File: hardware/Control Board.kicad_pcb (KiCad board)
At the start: 2 copper layers, 68.4 x 53.1 mm, 38 parts, among them J1 Conn_FTDI, J2 SOLAR, M1 Motor_DC, Q1 IRF7105PbF, Q2 BC817W, Q3 BC817W, Q4 IRF7105PbF, SW1 SW_Push, SW2 SW_Push, SW3 SW_Push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

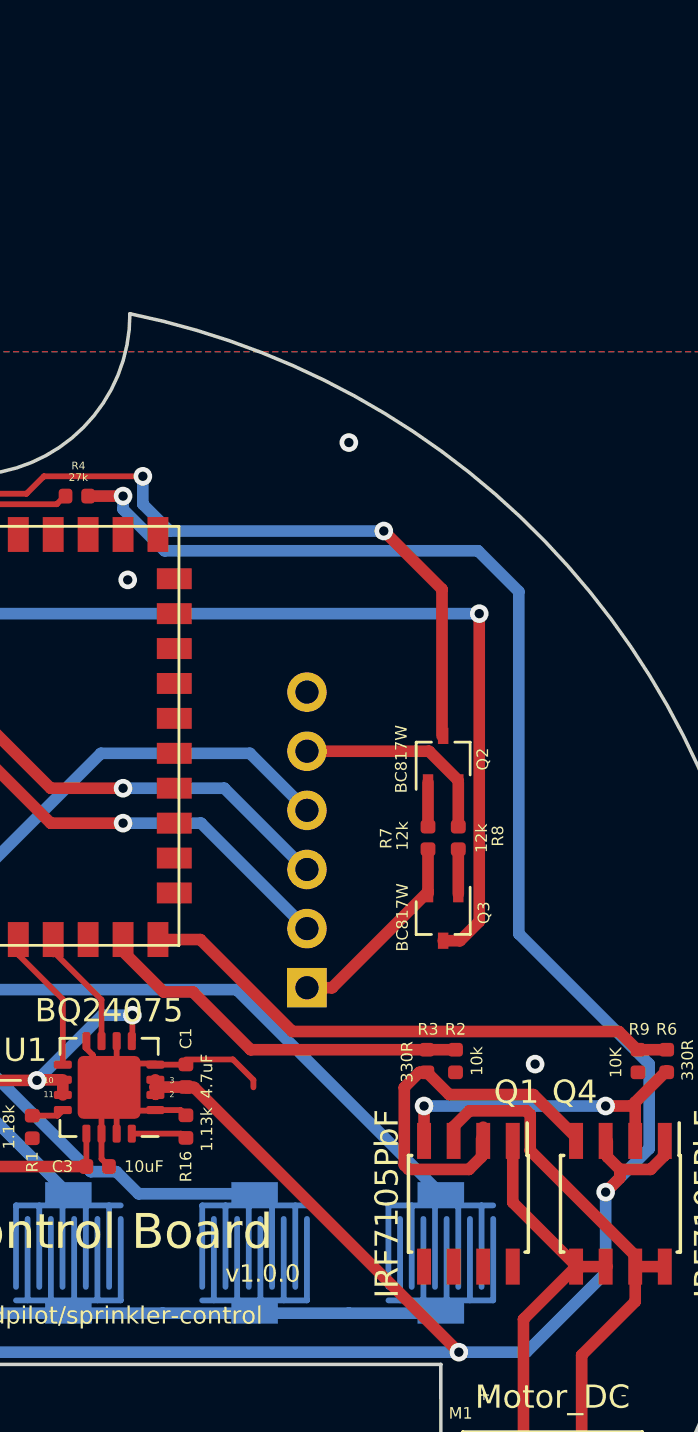
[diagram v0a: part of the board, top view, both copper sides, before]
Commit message: Add pull up resistors on the auto programmer circuit, switch the RX and TX lines
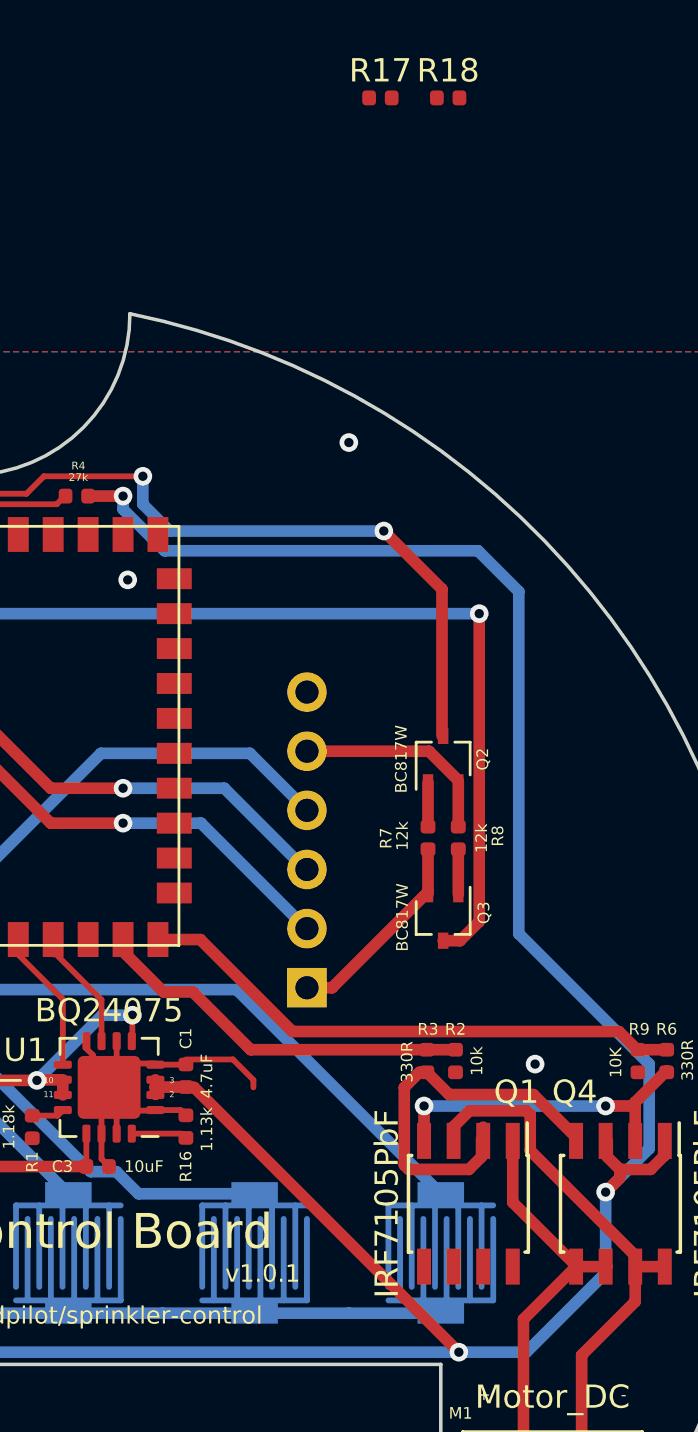
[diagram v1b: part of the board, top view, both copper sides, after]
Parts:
- added R17: 10k, Resistor_SMD:R_0402_1005Metric, F.Cu at (126.7, 87.6)
- added R18: 10k, Resistor_SMD:R_0402_1005Metric, F.Cu at (129.6, 87.6)
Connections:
- U3 pad 37: TX -> RX
- U3 pad 38: RX -> TX
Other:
- board text added: "v1.0.1"
- board text removed: "v1.0.0"
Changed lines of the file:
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@@
     (tracks 258)
     (zones 0)
-    (modules 38)
+    (modules 40)
     (nets 54)
   )
@@
     (add_net WATER_ON)
   )
+  (module Resistor_SMD:R_0402_1005Metric (layer F.Cu)
+    (at 129.565001 87.595001)
+    (descr "Resistor SMD 0402 (1005 Metric), square (rectangular) end terminal, IPC_7351 nominal, (Body size source: http://www.tortai-tech.com/upload/download/2011102023233369053.pdf), generated with kicad-footprint-generator")
+    (tags resistor)
+    (attr smd)
+    (fp_text reference R18 (at 0 -1.17) (layer F.SilkS)
+      (effects (font (size 1 1) (thickness 0.15)))
+    )
+    (fp_text value 10k (at 0 1.17) (layer F.Fab)
+      (effects (font (size 1 1) (thickness 0.15)))
+    )
+    (fp_text user %R (at 0 0) (layer F.Fab)
+      (effects (font (size 0.25 0.25) (thickness 0.04)))
+    )
+    (fp_line (start -0.5 0.25) (end -0.5 -0.25) (layer F.Fab) (width 0.1))
+    (fp_line (start -0.5 -0.25) (end 0.5 -0.25) (layer F.Fab) (width 0.1))
+    (fp_line (start 0.5 -0.25) (end 0.5 0.25) (layer F.Fab) (width 0.1))
+    (fp_line (start 0.5 0.25) (end -0.5 0.25) (layer F.Fab) (width 0.1))
+    (fp_line (start -0.93 0.47) (end -0.93 -0.47) (layer F.CrtYd) (width 0.05))
+    (fp_line (start -0.93 -0.47) (end 0.93 -0.47) (layer F.CrtYd) (width 0.05))
+    (fp_line (start 0.93 -0.47) (end 0.93 0.47) (layer F.CrtYd) (width 0.05))
+    (fp_line (start 0.93 0.47) (end -0.93 0.47) (layer F.CrtYd) (width 0.05))
+    (pad 2 smd roundrect (at 0.485 0) (size 0.59 0.64) (layers F.Cu F.Paste F.Mask) (roundrect_rratio 0.25)
+      (net 9 EN))
+    (pad 1 smd roundrect (at -0.485 0) (size 0.59 0.64) (layers F.Cu F.Paste F.Mask) (roundrect_rratio 0.25)
+      (net 3 +3V3))
+    (model ${KISYS3DMOD}/Resistor_SMD.3dshapes/R_0402_1005Metric.wrl
+      (at (xyz 0 0 0))
+      (scale (xyz 1 1 1))
+      (rotate (xyz 0 0 0))
+    )
+  )
+  (module Resistor_SMD:R_0402_1005Metric (layer F.Cu)
+    (at 126.655001 87.595001)
+    (descr "Resistor SMD 0402 (1005 Metric), square (rectangular) end terminal, IPC_7351 nominal, (Body size source: http://www.tortai-tech.com/upload/download/2011102023233369053.pdf), generated with kicad-footprint-generator")
+    (tags resistor)
+    (attr smd)
+    (fp_text reference R17 (at 0 -1.17) (layer F.SilkS)
+      (effects (font (size 1 1) (thickness 0.15)))
+    )
+    (fp_text value 10k (at 0 1.17) (layer F.Fab)
+      (effects (font (size 1 1) (thickness 0.15)))
+    )
+    (fp_text user %R (at 0 0) (layer F.Fab)
+      (effects (font (size 0.25 0.25) (thickness 0.04)))
+    )
+    (fp_line (start -0.5 0.25) (end -0.5 -0.25) (layer F.Fab) (width 0.1))
+    (fp_line (start -0.5 -0.25) (end 0.5 -0.25) (layer F.Fab) (width 0.1))
+    (fp_line (start 0.5 -0.25) (end 0.5 0.25) (layer F.Fab) (width 0.1))
+    (fp_line (start 0.5 0.25) (end -0.5 0.25) (layer F.Fab) (width 0.1))
+    (fp_line (start -0.93 0.47) (end -0.93 -0.47) (layer F.CrtYd) (width 0.05))
+    (fp_line (start -0.93 -0.47) (end 0.93 -0.47) (layer F.CrtYd) (width 0.05))
+    (fp_line (start 0.93 -0.47) (end 0.93 0.47) (layer F.CrtYd) (width 0.05))
+    (fp_line (start 0.93 0.47) (end -0.93 0.47) (layer F.CrtYd) (width 0.05))
+    (pad 2 smd roundrect (at 0.485 0) (size 0.59 0.64) (layers F.Cu F.Paste F.Mask) (roundrect_rratio 0.25)
+      (net 10 IO0))
+    (pad 1 smd roundrect (at -0.485 0) (size 0.59 0.64) (layers F.Cu F.Paste F.Mask) (roundrect_rratio 0.25)
+      (net 3 +3V3))
+    (model ${KISYS3DMOD}/Resistor_SMD.3dshapes/R_0402_1005Metric.wrl
+      (at (xyz 0 0 0))
+      (scale (xyz 1 1 1))
+      (rotate (xyz 0 0 0))
+    )
+  )
   (module Package_DFN_QFN:Texas_S-PVQFN-N16_EP2.7x2.7mm (layer F.Cu)
     (at 115 130.1 180)
@@
       (net 39 "Net-(R11-Pad2)"))
     (pad 37 smd rect (at 8.65 -0.4 90) (size 1.5 0.9) (layers F.Cu F.Paste F.Mask)
-      (net 29 TX))
+      (net 30 RX))
     (pad 6 smd rect (at -8.75 -0.4 90) (size 1.5 0.9) (layers F.Cu F.Paste F.Mask)
       (net 38 "Net-(R10-Pad2)"))
     (pad 38 smd rect (at 8.65 -1.9 90) (size 1.5 0.9) (layers F.Cu F.Paste F.Mask)
-      (net 30 RX))
+      (net 29 TX))
     (pad 5 smd rect (at -8.75 -1.9 90) (size 1.5 0.9) (layers F.Cu F.Paste F.Mask)
       (net 16 "Net-(U3-Pad5)"))
@@
     (effects (font (size 0.75 0.75) (thickness 0.15)))
   )
-  (gr_text v1.0.0 (at 121.6 138.1) (layer F.SilkS)
+  (gr_text v1.0.1 (at 121.6 138.1) (layer F.SilkS)
     (effects (font (size 0.75 0.75) (thickness 0.15)))
   )

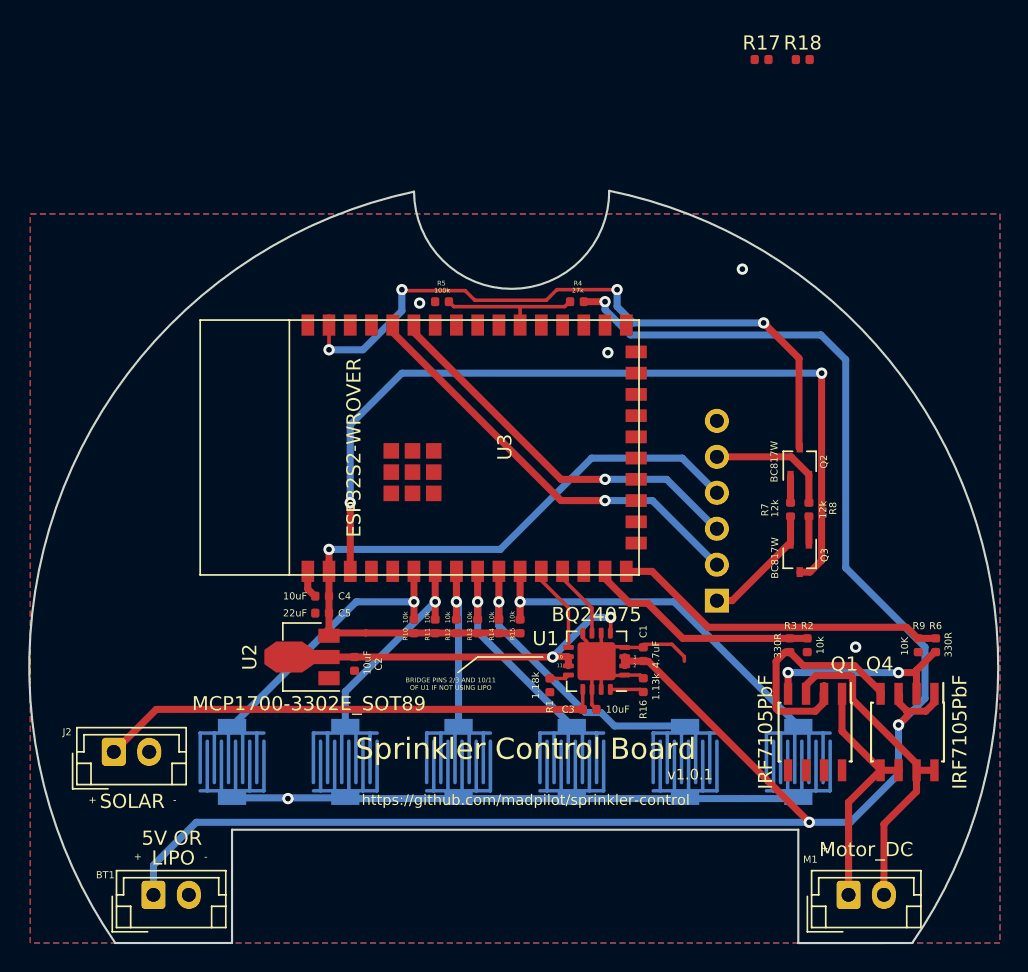
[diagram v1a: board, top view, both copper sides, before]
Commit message: Placing the pull ups on the programmer
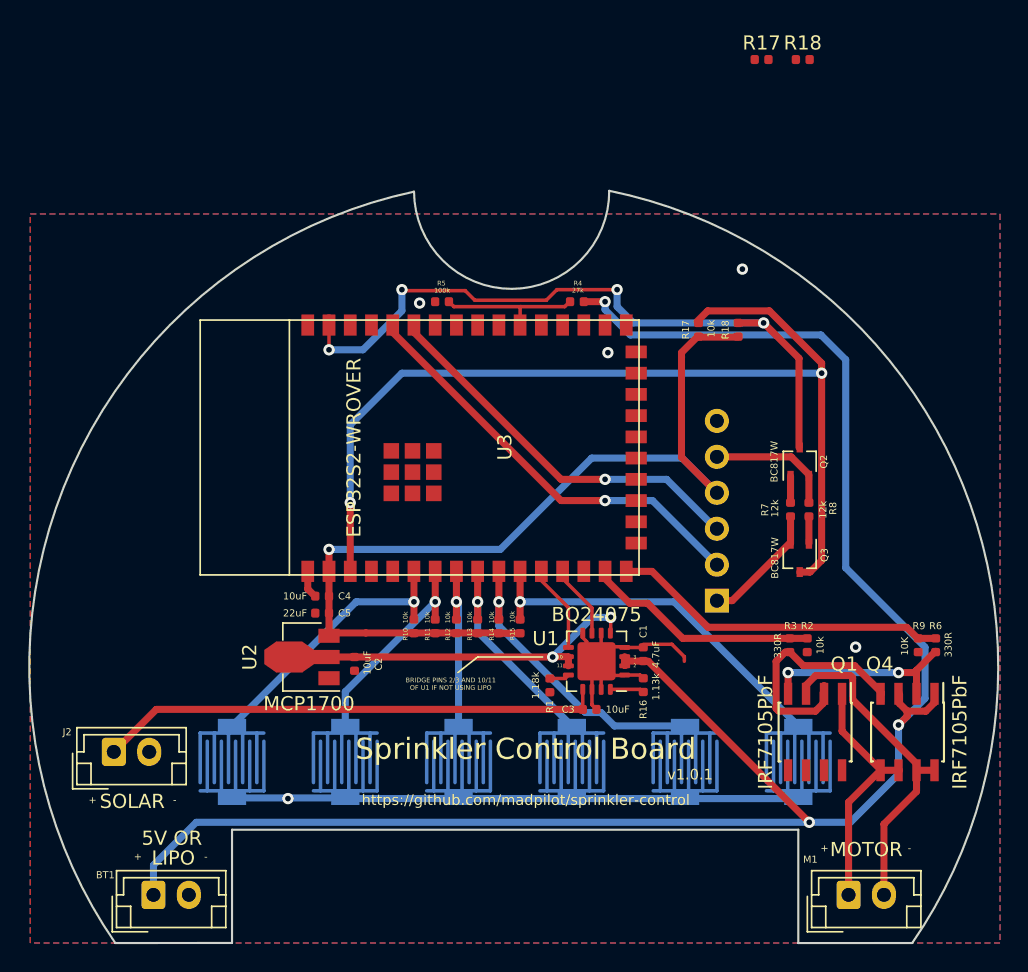
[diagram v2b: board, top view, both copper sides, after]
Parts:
- added R17: 10k, Resistor_SMD:R_0402_1005Metric, F.Cu at (122.2, 106.7)
- added R18: 10k, Resistor_SMD:R_0402_1005Metric, F.Cu at (125.0, 106.7)
- M1: value Motor_DC -> MOTOR
- U2: value MCP1700-3302E_SOT89 -> MCP1700
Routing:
- net +3V3: track 50.8 -> 66.2 mm
- net IO0: track 60.3 -> 71.6 mm
- net EN: track 47.7 -> 49.5 mm
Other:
- board text added: "RX TX"
- board text added: "TX RX"
- board text removed: "RX"
- board text removed: "TX"
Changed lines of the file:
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@@
   (general
     (thickness 1.6)
-    (drawings 47)
-    (tracks 258)
+    (drawings 57)
+    (tracks 268)
     (zones 0)
     (modules 40)
@@
   )
   (setup
-    (last_trace_width 0.25)
+    (last_trace_width 0.5)
     (user_trace_width 0.5)
     (trace_clearance 0.2)
@@
       (effects (font (size 1 1) (thickness 0.15)))
     )
-    (fp_text value MCP1700-3302E_SOT89 (at -0.0665 -3.3 180) (layer F.SilkS)
+    (fp_text value MCP1700 (at -0.0665 -3.3 180) (layer F.SilkS)
       (effects (font (size 1 1) (thickness 0.15)))
     )
@@
       (effects (font (size 0.5 0.5) (thickness 0.1)))
     )
-    (fp_text value Motor_DC (at 1.25 -3.2) (layer F.SilkS)
+    (fp_text value MOTOR (at 1.25 -3.2) (layer F.SilkS)
       (effects (font (size 1 1) (thickness 0.15)))
     )
@@
     )
   )
+  (module Resistor_SMD:R_0402_1005Metric (layer F.Cu)
+    (at 122.2 106.685 90)
+    (descr "Resistor SMD 0402 (1005 Metric), square (rectangular) end terminal, IPC_7351 nominal, (Body size source: http://www.tortai-tech.com/upload/download/2011102023233369053.pdf), generated with kicad-footprint-generator")
+    (tags resistor)
+    (attr smd)
+    (fp_text reference R17 (at 0 -0.9 90) (layer F.SilkS)
+      (effects (font (size 0.5 0.5) (thickness 0.125)))
+    )
+    (fp_text value 10k (at 0.085 0.9 90) (layer F.SilkS)
+      (effects (font (size 0.5 0.5) (thickness 0.125)))
+    )
+    (fp_line (start 0.93 0.47) (end -0.93 0.47) (layer F.CrtYd) (width 0.05))
+    (fp_line (start 0.93 -0.47) (end 0.93 0.47) (layer F.CrtYd) (width 0.05))
+    (fp_line (start -0.93 -0.47) (end 0.93 -0.47) (layer F.CrtYd) (width 0.05))
+    (fp_line (start -0.93 0.47) (end -0.93 -0.47) (layer F.CrtYd) (width 0.05))
+    (fp_line (start 0.5 0.25) (end -0.5 0.25) (layer F.Fab) (width 0.1))
+    (fp_line (start 0.5 -0.25) (end 0.5 0.25) (layer F.Fab) (width 0.1))
+    (fp_line (start -0.5 -0.25) (end 0.5 -0.25) (layer F.Fab) (width 0.1))
+    (fp_line (start -0.5 0.25) (end -0.5 -0.25) (layer F.Fab) (width 0.1))
+    (fp_text user %R (at 0 0 90) (layer F.Fab)
+      (effects (font (size 0.25 0.25) (thickness 0.04)))
+    )
+    (pad 1 smd roundrect (at -0.485 0 90) (size 0.59 0.64) (layers F.Cu F.Paste F.Mask) (roundrect_rratio 0.25)
+      (net 3 +3V3))
+    (pad 2 smd roundrect (at 0.485 0 90) (size 0.59 0.64) (layers F.Cu F.Paste F.Mask) (roundrect_rratio 0.25)
+      (net 10 IO0))
+    (model ${KISYS3DMOD}/Resistor_SMD.3dshapes/R_0402_1005Metric.wrl
+      (at (xyz 0 0 0))
+      (scale (xyz 1 1 1))
+      (rotate (xyz 0 0 0))
+    )
+  )
+  (module Resistor_SMD:R_0402_1005Metric (layer F.Cu)
+    (at 125 106.685 90)
+    (descr "Resistor SMD 0402 (1005 Metric), square (rectangular) end terminal, IPC_7351 nominal, (Body size source: http://www.tortai-tech.com/upload/download/2011102023233369053.pdf), generated with kicad-footprint-generator")
+    (tags resistor)
+    (attr smd)
+    (fp_text reference R18 (at 0 -0.9 90) (layer F.SilkS)
+      (effects (font (size 0.5 0.5) (thickness 0.125)))
+    )
+    (fp_text value 10k (at 0.085 0.9 90) (layer B.Paste)
+      (effects (font (size 0.5 0.5) (thickness 0.125)))
+    )
+    (fp_text user %R (at 0 0 90) (layer F.Fab)
+      (effects (font (size 0.25 0.25) (thickness 0.04)))
+    )
+    (fp_line (start -0.5 0.25) (end -0.5 -0.25) (layer F.Fab) (width 0.1))
+    (fp_line (start -0.5 -0.25) (end 0.5 -0.25) (layer F.Fab) (width 0.1))
+    (fp_line (start 0.5 -0.25) (end 0.5 0.25) (layer F.Fab) (width 0.1))
+    (fp_line (start 0.5 0.25) (end -0.5 0.25) (layer F.Fab) (width 0.1))
+    (fp_line (start -0.93 0.47) (end -0.93 -0.47) (layer F.CrtYd) (width 0.05))
+    (fp_line (start -0.93 -0.47) (end 0.93 -0.47) (layer F.CrtYd) (width 0.05))
+    (fp_line (start 0.93 -0.47) (end 0.93 0.47) (layer F.CrtYd) (width 0.05))
+    (fp_line (start 0.93 0.47) (end -0.93 0.47) (layer F.CrtYd) (width 0.05))
+    (pad 2 smd roundrect (at 0.485 0 90) (size 0.59 0.64) (layers F.Cu F.Paste F.Mask) (roundrect_rratio 0.25)
+      (net 9 EN))
+    (pad 1 smd roundrect (at -0.485 0 90) (size 0.59 0.64) (layers F.Cu F.Paste F.Mask) (roundrect_rratio 0.25)
+      (net 3 +3V3))
+    (model ${KISYS3DMOD}/Resistor_SMD.3dshapes/R_0402_1005Metric.wrl
+      (at (xyz 0 0 0))
+      (scale (xyz 1 1 1))
+      (rotate (xyz 0 0 0))
+    )
+  )
+  (gr_line (start 120.5 123.4) (end 120.3 123.2) (layer B.SilkS) (width 0.12))
+  (gr_line (start 119.9 123.4) (end 120.5 123.4) (layer B.SilkS) (width 0.12))
+  (gr_line (start 120.5 123.4) (end 120.3 123.6) (layer B.SilkS) (width 0.12))
+  (gr_line (start 119.9 123.4) (end 120.1 123.2) (layer B.SilkS) (width 0.12))
+  (gr_line (start 119.9 123.4) (end 120.1 123.6) (layer B.SilkS) (width 0.12))
+  (gr_line (start 120 120.8) (end 120.2 121) (layer B.SilkS) (width 0.12))
+  (gr_line (start 120 120.8) (end 120.2 120.6) (layer B.SilkS) (width 0.12))
+  (gr_line (start 120.6 120.8) (end 120.4 121) (layer B.SilkS) (width 0.12))
+  (gr_line (start 120.6 120.8) (end 120.4 120.6) (layer B.SilkS) (width 0.12))
+  (gr_line (start 120 120.8) (end 120.6 120.8) (layer B.SilkS) (width 0.12))
   (gr_text 2 (at 117.7 130.4) (layer F.SilkS)
     (effects (font (size 0.26 0.25) (thickness 0.0625)))
@@
     (effects (font (size 0.5 0.5) (thickness 0.0625)) (justify mirror))
   )
-  (gr_text RX (at 121.3 123.4 90) (layer B.SilkS)
+  (gr_text "TX\n\nRX" (at 120.2 123.4 90) (layer B.SilkS)
     (effects (font (size 0.5 0.5) (thickness 0.0625)) (justify mirror))
   )
-  (gr_text TX (at 121.3 120.8 90) (layer B.SilkS)
+  (gr_text "RX\n\nTX" (at 120.3 120.8 90) (layer B.SilkS)
     (effects (font (size 0.5 0.5) (thickness 0.0625)) (justify mirror))
   )
@@
   (segment (start 98.7 128.1) (end 96.3 128.1) (width 0.5) (layer F.Cu) (net 3))
   (segment (start 96.3 128.1) (end 96.1 128.3) (width 0.5) (layer F.Cu) (net 3))
+  (segment (start 123.5 118.2) (end 121 115.7) (width 0.5) (layer F.Cu) (net 3))
+  (segment (start 121 115.7) (end 121 108.6) (width 0.5) (layer F.Cu) (net 3))
+  (segment (start 121 108.6) (end 121 108.3) (width 0.5) (layer F.Cu) (net 3))
+  (segment (start 121 108.3) (end 122.1 107.2) (width 0.5) (layer F.Cu) (net 3))
+  (segment (start 122.1 107.2) (end 125 107.2) (width 0.5) (layer F.Cu) (net 3))
   (via (at 128.53 130.9) (size 0.8) (drill 0.4) (layers F.Cu B.Cu) (net 4))
   (via (at 136.33 130.9) (size 0.8) (drill 0.4) (layers F.Cu B.Cu) (net 4))
@@
   (segment (start 112.2 103.849999) (end 116.450001 103.849999) (width 0.25) (layer F.Cu) (net 9))
   (segment (start 106.4 104.6) (end 111.449999 104.6) (width 0.25) (layer F.Cu) (net 9))
+  (segment (start 125 106.2) (end 126.8 106.2) (width 0.5) (layer F.Cu) (net 9))
   (via (at 130.9 109.75) (size 0.8) (drill 0.4) (layers F.Cu B.Cu) (net 10))
   (via (at 97.6 118.9) (size 0.8) (drill 0.4) (layers F.Cu B.Cu) (net 10))
@@
   (segment (start 101.25 109.75) (end 97.6 113.4) (width 0.5) (layer B.Cu) (net 10))
   (segment (start 130.9 109.75) (end 101.25 109.75) (width 0.5) (layer B.Cu) (net 10))
+  (segment (start 127.208001 105.349999) (end 122.850001 105.349999) (width 0.5) (layer F.Cu) (net 10))
+  (segment (start 130.9 109.041998) (end 127.208001 105.349999) (width 0.5) (layer F.Cu) (net 10))
+  (segment (start 130.9 109.75) (end 130.9 109.041998) (width 0.5) (layer F.Cu) (net 10))
+  (segment (start 122.850001 105.349999) (end 122.1 106.1) (width 0.5) (layer F.Cu) (net 10))
   (segment (start 128.7 119.87) (end 128.7 121.8) (width 0.5) (layer F.Cu) (net 11))
   (segment (start 123.5 125.82) (end 124.58 125.82) (width 0.5) (layer F.Cu) (net 11))
